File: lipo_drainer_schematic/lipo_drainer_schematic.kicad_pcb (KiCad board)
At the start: 2 copper layers, 58 parts, among them J1 BATT, J2 FAN, J3 Vcal, J4 128x64_OLED, J5 Gcal, J6 Ical, Q1 MMBT3904, Q10 G700P06T, Q11 G700P06T, Q2 IRLML5103TRPBF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

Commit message: Added temperature sensor
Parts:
- added J7: Heatsink Temp (for MCP7901), Connector_PinHeader_2.54mm:PinHeader_1x03_P2.54mm_Vertical, F.Cu at (166.5, 93.9)
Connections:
- net /ADC renamed /VOLT
- C2 pad 1: /3.3V -> /VSYS
- J4 pad 1: /3.3V -> /3V3
- R7 pad 2: Net-(U2-3V3) -> /3V3
- U2 pad 34: unconnected-(U2-GPIO28_ADC2-Pad34) -> /TEMP
- U2 pad 36: Net-(U2-3V3) -> /3V3
- U2 pad 39: /3.3V -> /VSYS
- U3 pad 5: /3.3V -> /VSYS
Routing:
- net Net-(J6-Pin_2): track 163.0 -> 187.2 mm

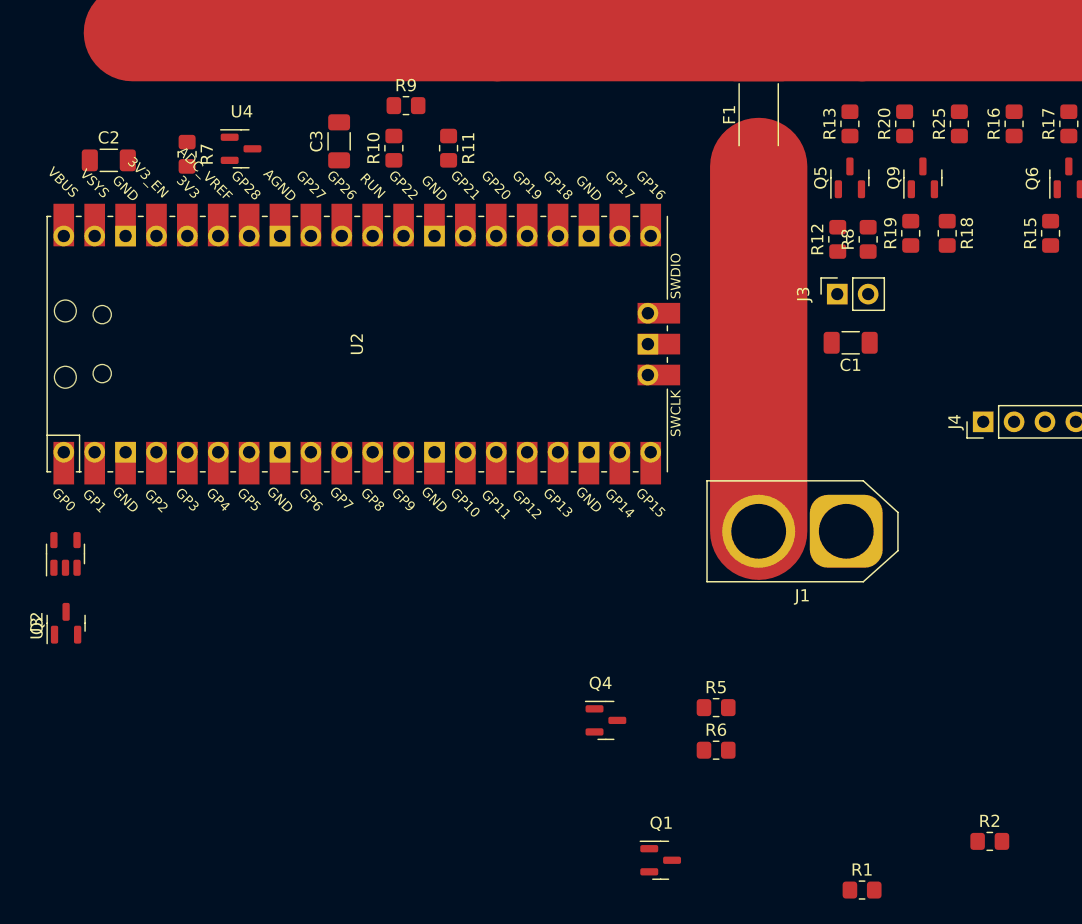
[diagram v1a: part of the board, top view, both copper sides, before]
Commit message: Added more net labels
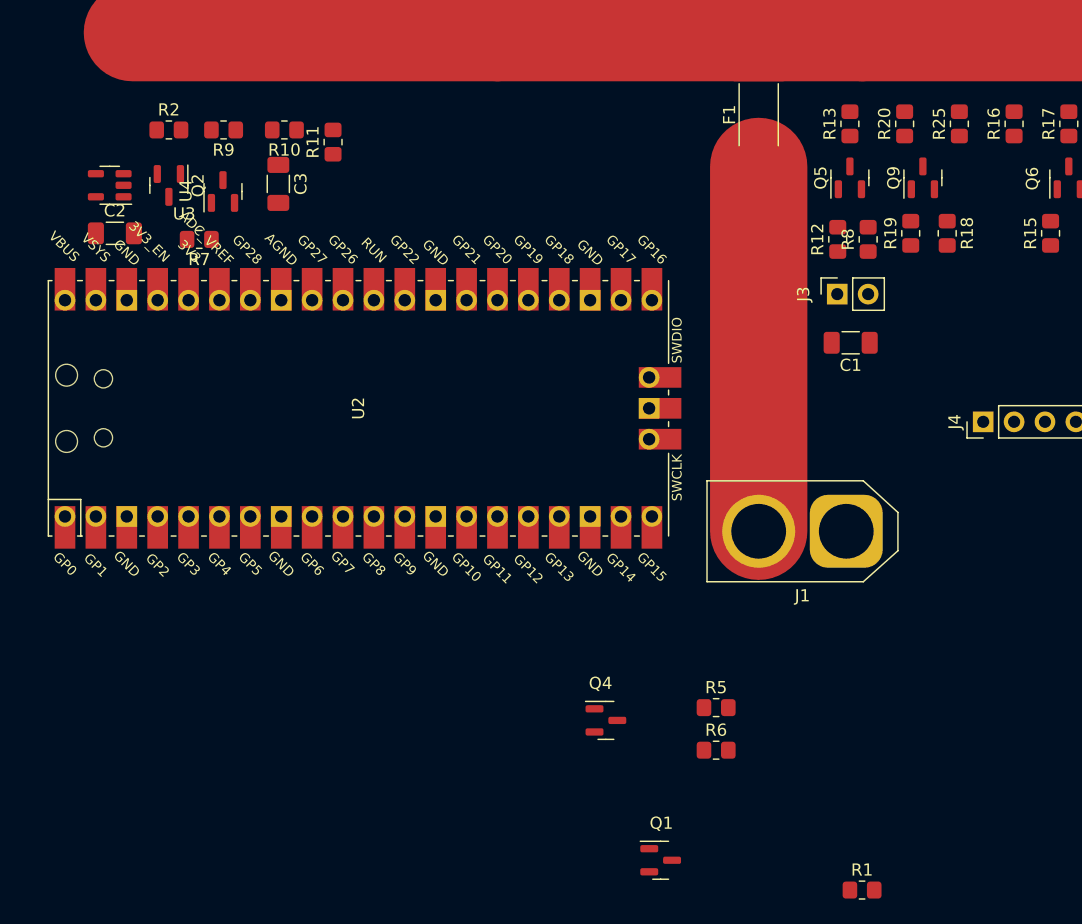
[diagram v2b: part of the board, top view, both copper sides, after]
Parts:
- moved R2 89.3 mm to (59.0, 105.5)
- moved Q2 37.0 mm to (59.0, 110.1), turned to -90 degrees
- moved U3 30.5 mm to (54.1, 110.0), turned to 180 degrees
- moved R9 15.1 mm to (63.5, 105.5), turned to 180 degrees
- moved R11 9.51 mm to (72.5, 106.5), turned to 90 degrees
- moved R10 9.12 mm to (68.5, 105.5), turned to 180 degrees
- moved R7 7.07 mm to (61.5, 114.5), turned to 180 degrees
- moved C3 6.10 mm to (68.0, 109.9), turned to -90 degrees
- moved C2 6.02 mm to (54.6, 114.0)
- moved U2 5.28 mm to (74.6, 128.4)
- moved U4 3.81 mm to (63.5, 110.6), turned to 90 degrees
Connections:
- net Net-(D1-K) renamed /FAN+
- net Net-(J3-Pin_2) renamed /VHIGH
- net Net-(J5-Pin_2) renamed /FET-G
- net Net-(J6-Pin_2) renamed /FET-D
- net Net-(Q1-C) renamed /ON
- net Net-(Q10-S) renamed /FET-S

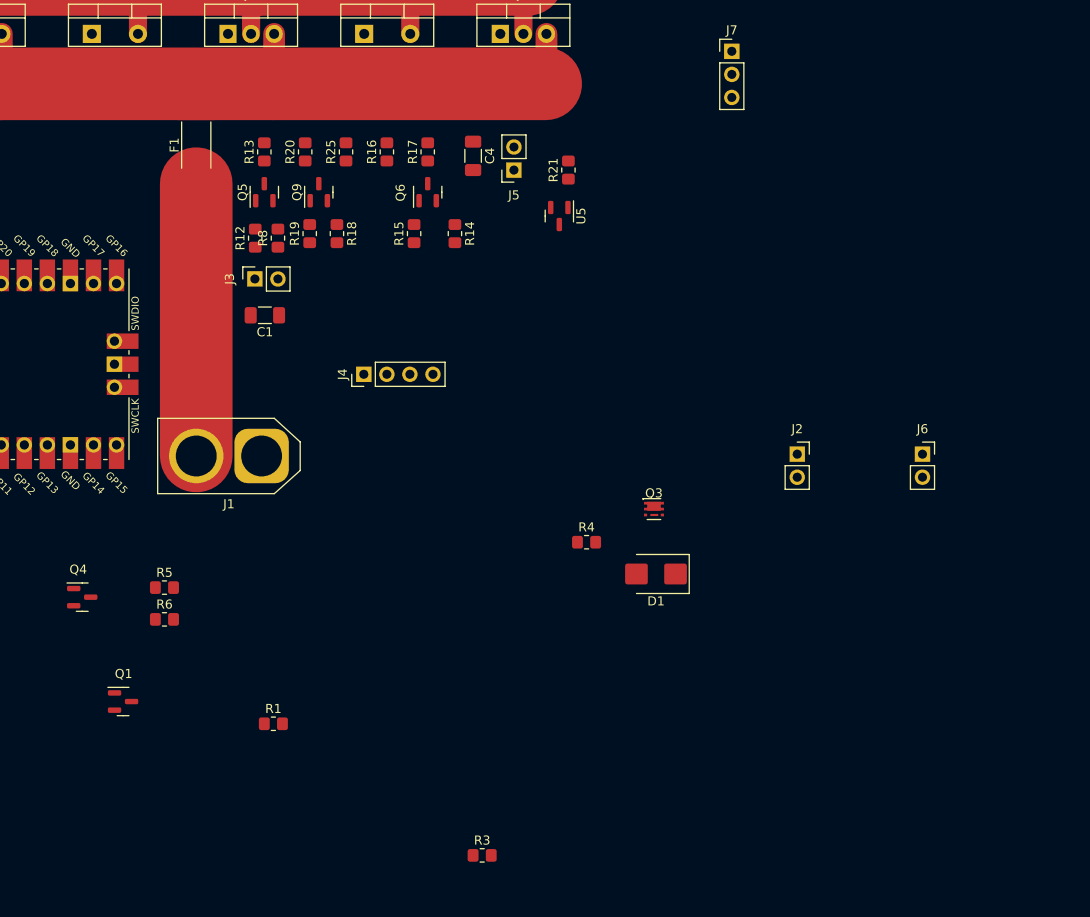
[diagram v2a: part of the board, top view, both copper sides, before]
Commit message: Added OLED footprint
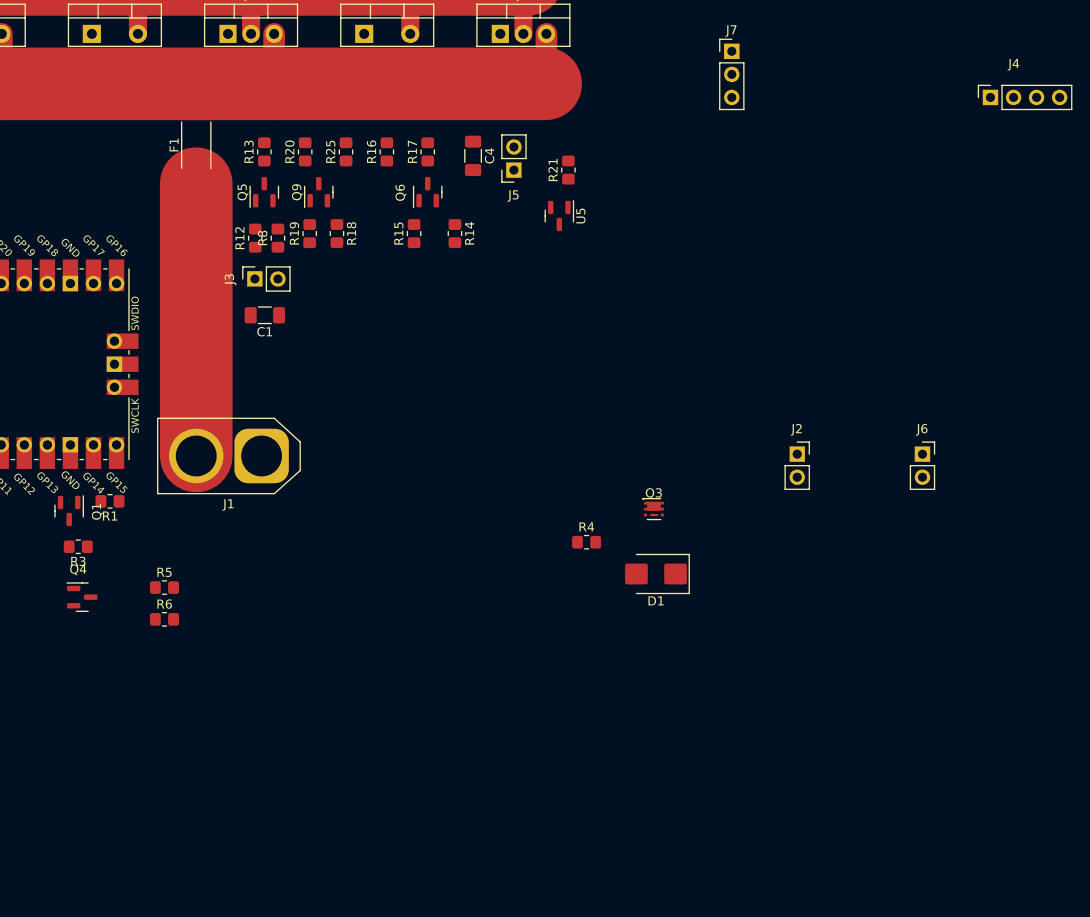
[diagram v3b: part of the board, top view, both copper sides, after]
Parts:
- J4: footprint Connector_PinHeader_2.54mm:PinHeader_1x04_P2.54mm_Vertical -> Matt:OLED_128_64_1.3in
- moved J4 75.5 mm to (195.0, 99.0), turned to 0 degrees
- moved R3 56.0 mm to (94.5, 148.5), turned to 180 degrees
- moved R1 30.4 mm to (98.0, 143.5), turned to 180 degrees
- moved Q1 21.8 mm to (93.5, 144.6), turned to -90 degrees
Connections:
- J4 pad 1: /3V3 -> GND
- J4 pad 2: GND -> /3V3

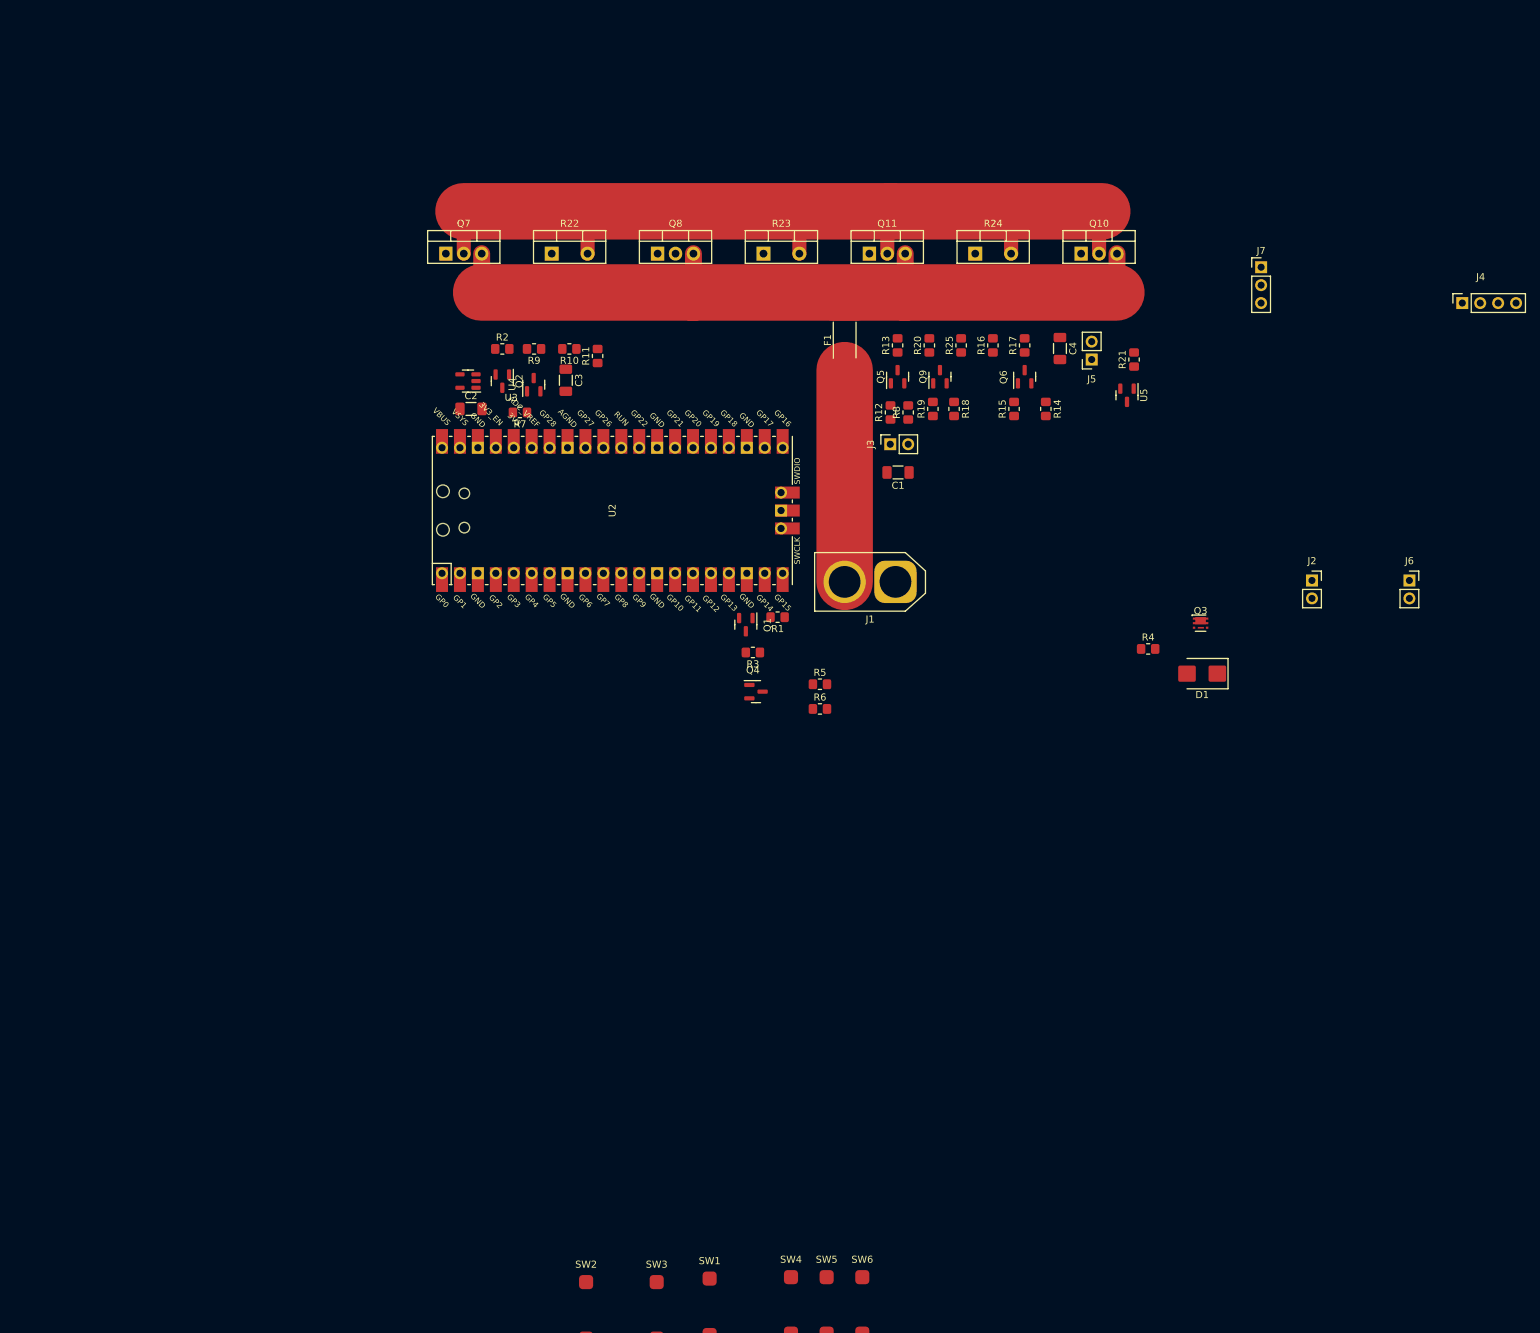
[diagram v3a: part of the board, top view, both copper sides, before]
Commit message: Change XT-60 connecter
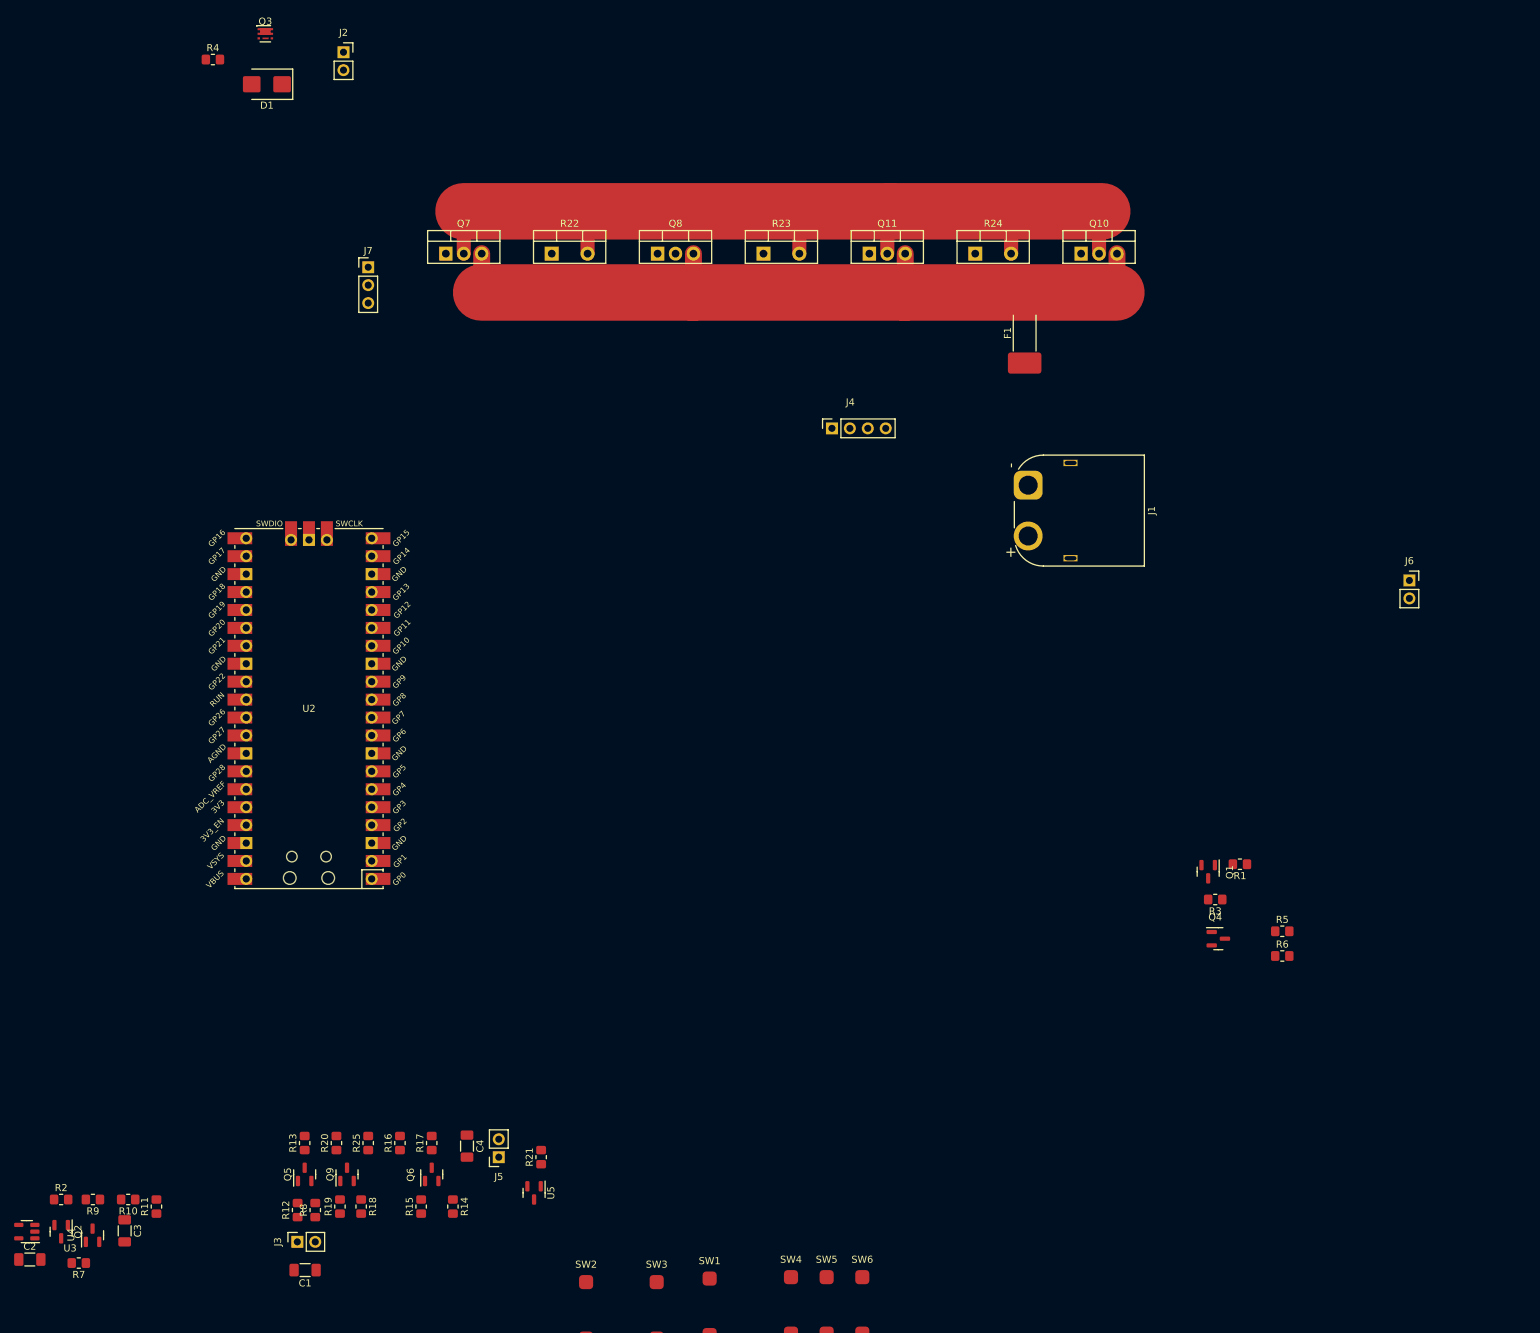
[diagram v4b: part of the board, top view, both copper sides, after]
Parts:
- J1: footprint Connector_AMASS:AMASS_XT60-M_1x02_P7.20mm_Vertical -> Connector_AMASS:AMASS_XT60PW-M_1x02_P7.20mm_Horizontal
- moved D1 156.6 mm to (25.6, 68.0)
- moved Q3 156.6 mm to (25.4, 60.9)
- moved R4 156.6 mm to (18.0, 64.5)
- moved J2 156.3 mm to (36.5, 63.5)
- moved C1 140.8 mm to (31.1, 236.0)
- moved C4 140.8 mm to (54.0, 218.4)
- moved J3 140.8 mm to (30.0, 232.0)
- moved J5 140.8 mm to (58.5, 220.0)
- moved Q5 140.8 mm to (31.0, 222.4)
- moved Q6 140.8 mm to (49.0, 222.4)
- moved Q9 140.8 mm to (37.0, 222.4)
- moved R12 140.8 mm to (30.0, 227.5)
- moved R13 140.8 mm to (31.0, 218.0)
- moved R14 140.8 mm to (52.0, 227.0)
- moved R15 140.8 mm to (47.5, 227.0)
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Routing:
- net /BAT+: track 30.0 -> 0.00 mm
